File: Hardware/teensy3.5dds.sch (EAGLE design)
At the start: 101 parts, among them IC1 AD8034, IC10 AD8034, IC11 AD8034, IC12 AD8034, IC2 AD8034, IC4 AD737KRZ-R7, IC8 AD8034, IC9 AD8034, J1 1776275-2, J2 1776275-2, Q1 CSM-7X-DU, X1 1-227161-0

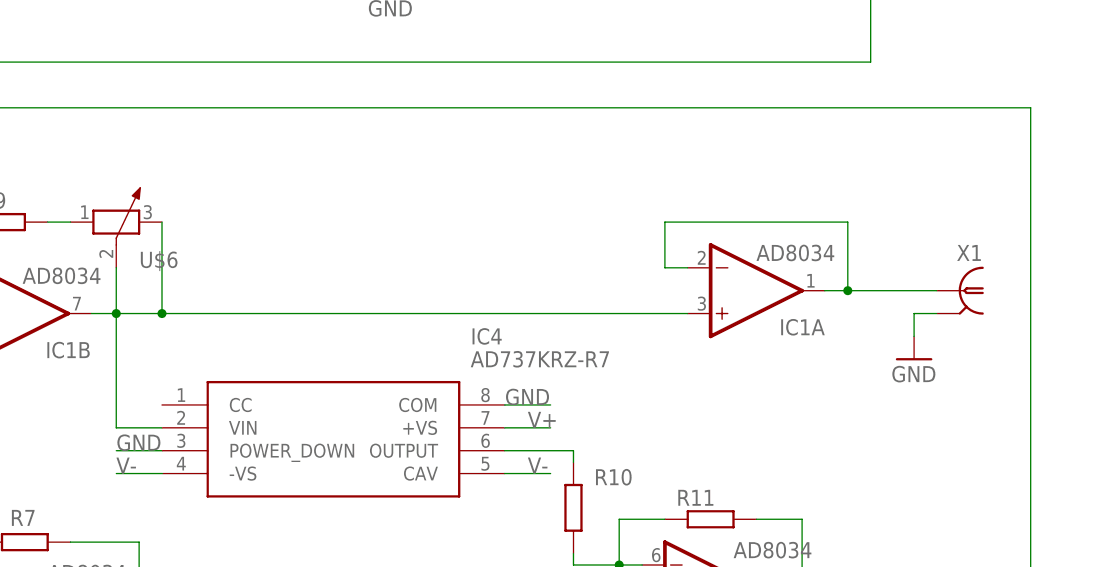
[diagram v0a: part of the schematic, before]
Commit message: hardware: add 50 Ohm resistor before BNC connector
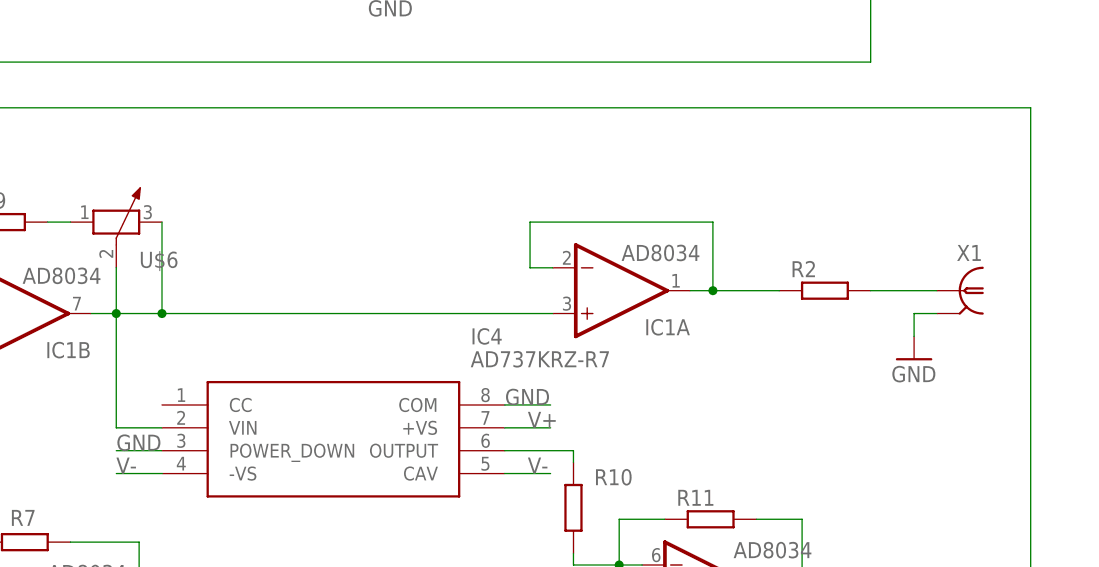
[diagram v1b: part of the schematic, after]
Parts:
- added R2: (no value), rcl:R-EU_R0805
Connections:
- new net N$6: R2.2, X1.1
- net N$19: now also R2.1; no longer X1.1
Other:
- moved on the sheet: IC1A
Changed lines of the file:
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@@
 <setting verticaltext="up"/>
 </settings>
-<grid distance="0.1" unitdist="inch" unit="inch" style="lines" multiple="1" display="yes" altdistance="0.05" altunitdist="inch" altunit="inch"/>
+<grid distance="0.1" unitdist="inch" unit="inch" style="lines" multiple="1" display="yes" altdistance="0.01" altunitdist="inch" altunit="inch"/>
 <layers>
 <layer number="1" name="Top" color="4" fill="1" visible="no" active="no"/>
@@
 <part name="GND10" library="supply1" library_urn="urn:adsk.eagle:library:371" deviceset="GND" device=""/>
 <part name="GND18" library="supply1" library_urn="urn:adsk.eagle:library:371" deviceset="GND" device=""/>
+<part name="R2" library="rcl" library_urn="urn:adsk.eagle:library:334" deviceset="R-EU_" device="R0805" package3d_urn="urn:adsk.eagle:package:23553/2"/>
 </parts>
 <sheets>
@@
 <attribute name="VALUE" x="35.56" y="-213.36" size="1.778" layer="96"/>
 </instance>
-<instance part="IC1" gate="A" x="322.58" y="-81.28" smashed="yes" rot="MR180">
-<attribute name="NAME" x="325.12" y="-84.455" size="1.778" layer="95" rot="MR180"/>
-<attribute name="VALUE" x="322.58" y="-76.2" size="1.778" layer="96" rot="MR180"/>
+<instance part="IC1" gate="A" x="307.594" y="-81.28" smashed="yes" rot="MR180">
+<attribute name="NAME" x="310.134" y="-84.455" size="1.778" layer="95" rot="MR180"/>
+<attribute name="VALUE" x="307.594" y="-76.2" size="1.778" layer="96" rot="MR180"/>
 </instance>
 <instance part="IC1" gate="B" x="241.046" y="-83.82" smashed="yes" rot="MR180">
@@
 <instance part="GND18" gate="1" x="-25.4" y="7.62" smashed="yes">
 <attribute name="VALUE" x="-27.94" y="5.08" size="1.778" layer="96"/>
+</instance>
+<instance part="R2" gate="G$1" x="330.2" y="-81.28" smashed="yes">
+<attribute name="NAME" x="326.39" y="-79.7814" size="1.778" layer="95"/>
+<attribute name="VALUE" x="326.39" y="-84.582" size="1.778" layer="96"/>
 </instance>
 </instances>
@@
 <wire x1="248.666" y1="-83.82" x2="251.46" y2="-83.82" width="0.1524" layer="91"/>
 <pinref part="IC1" gate="A" pin="+IN"/>
-<wire x1="256.54" y1="-83.82" x2="314.96" y2="-83.82" width="0.1524" layer="91"/>
+<wire x1="256.54" y1="-83.82" x2="299.974" y2="-83.82" width="0.1524" layer="91"/>
 <junction x="256.54" y="-83.82"/>
 </segment>
@@
 <segment>
 <pinref part="IC1" gate="A" pin="-IN"/>
-<wire x1="314.96" y1="-78.74" x2="312.42" y2="-78.74" width="0.1524" layer="91"/>
-<wire x1="312.42" y1="-78.74" x2="312.42" y2="-73.66" width="0.1524" layer="91"/>
+<wire x1="299.974" y1="-78.74" x2="297.434" y2="-78.74" width="0.1524" layer="91"/>
+<wire x1="297.434" y1="-78.74" x2="297.434" y2="-73.66" width="0.1524" layer="91"/>
+<pinref part="IC1" gate="A" pin="OUT"/>
+<wire x1="317.754" y1="-81.28" x2="315.214" y2="-81.28" width="0.1524" layer="91"/>
+<wire x1="297.434" y1="-73.66" x2="317.754" y2="-73.66" width="0.1524" layer="91"/>
+<wire x1="317.754" y1="-73.66" x2="317.754" y2="-81.28" width="0.1524" layer="91"/>
+<junction x="317.754" y="-81.28"/>
+<wire x1="325.12" y1="-81.28" x2="317.754" y2="-81.28" width="0.1524" layer="91"/>
+<pinref part="R2" gate="G$1" pin="1"/>
+</segment>
+</net>
+<net name="N$6" class="1">
+<segment>
 <pinref part="X1" gate="G$1" pin="1"/>
-<pinref part="IC1" gate="A" pin="OUT"/>
-<wire x1="342.646" y1="-81.28" x2="332.74" y2="-81.28" width="0.1524" layer="91"/>
-<wire x1="332.74" y1="-81.28" x2="330.2" y2="-81.28" width="0.1524" layer="91"/>
-<wire x1="312.42" y1="-73.66" x2="332.74" y2="-73.66" width="0.1524" layer="91"/>
-<wire x1="332.74" y1="-73.66" x2="332.74" y2="-81.28" width="0.1524" layer="91"/>
-<junction x="332.74" y="-81.28"/>
-</segment>
-</net>
+<wire x1="342.646" y1="-81.28" x2="335.28" y2="-81.28" width="0.1524" layer="91"/>
+<pinref part="R2" gate="G$1" pin="2"/>
+</segment>
+</net>

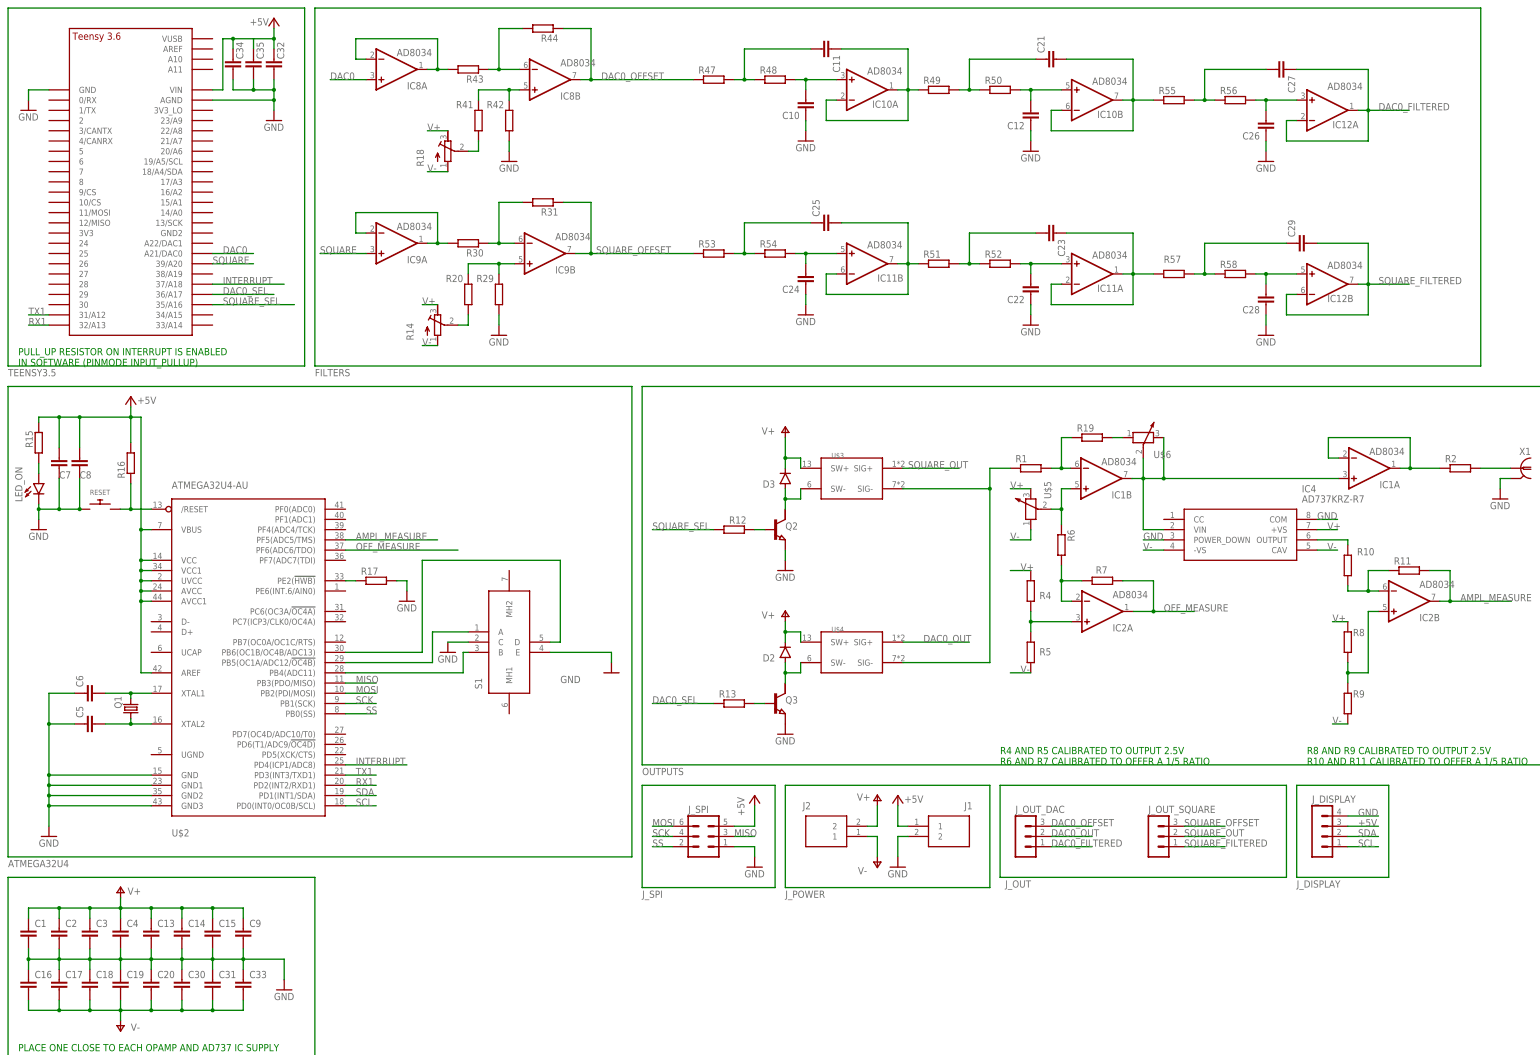
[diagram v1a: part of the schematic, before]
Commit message: hardware: renumber parts * Label power connector on board
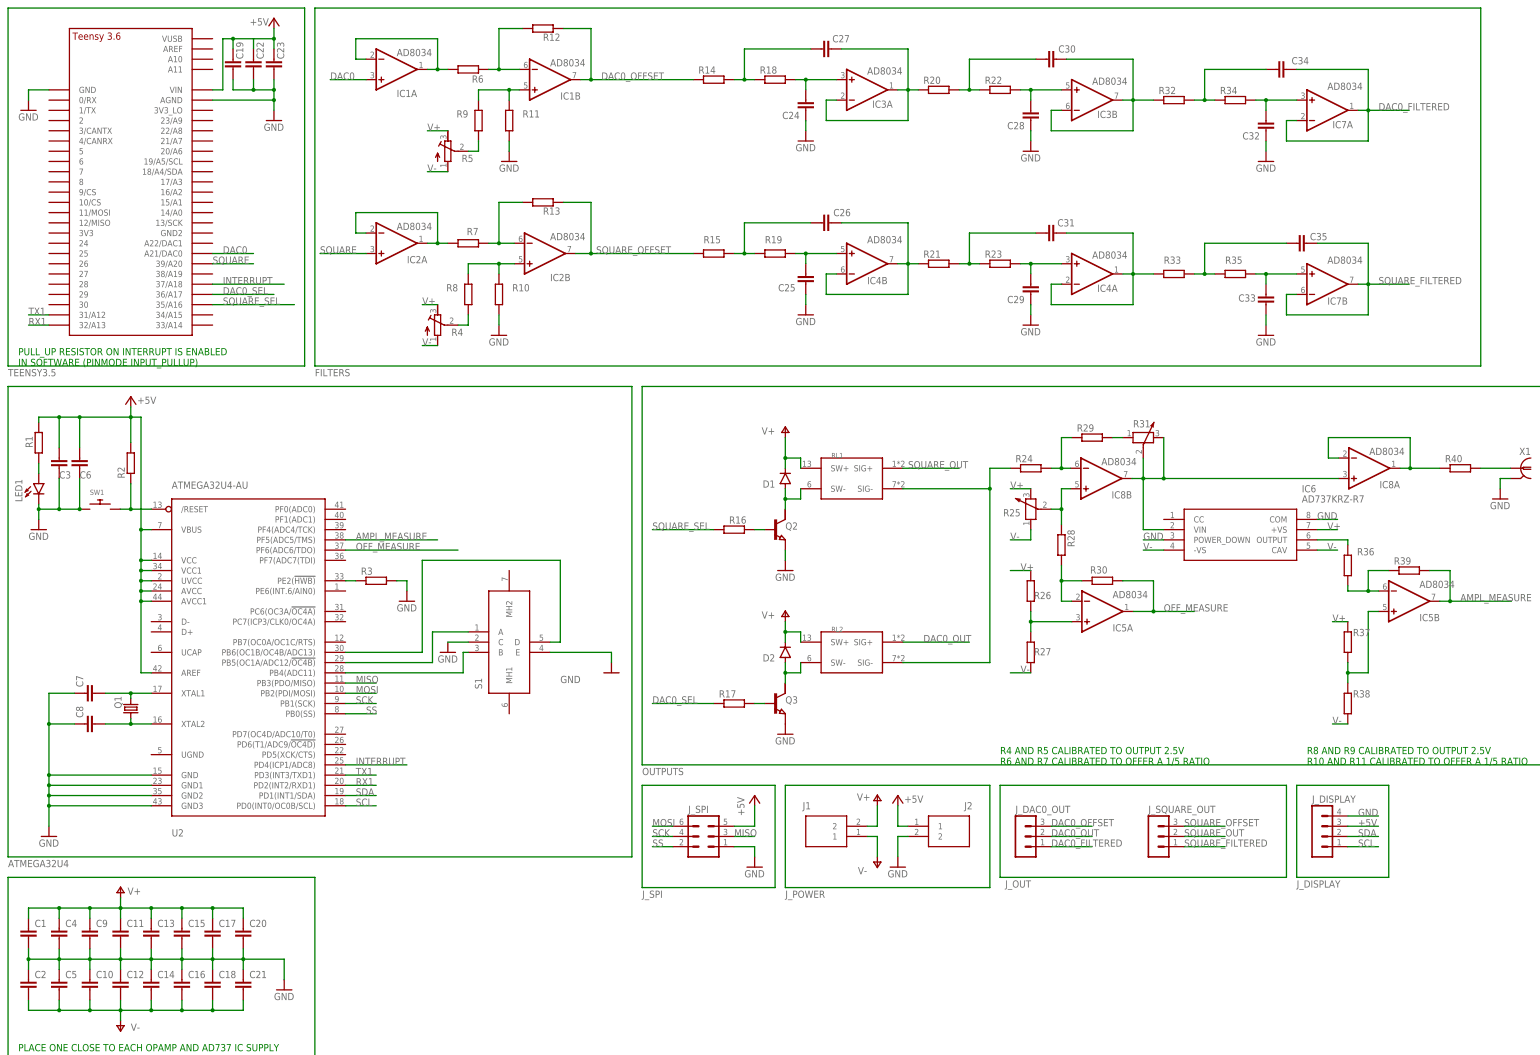
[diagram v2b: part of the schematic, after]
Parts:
- removed IC11, IC9: AD8034, linear:TL082D
- removed R41, R42, R43, R44, R47, R48: (no value), rcl:R-EU_R0805
- removed R49, R53, R54: (no value), rcl:R-EU_M0805
- removed U$6: POTENTIOMETER_VERTICAL, Potentiometer_vertical:POTENTIOMETER_VERTICAL
- added IC5: AD8034, linear:TL082D
- added IC6: AD737KRZ-R7, AD737KRZ-R7:AD737KRZ-R7
- added R24, R26, R27, R28, R36, R37, R38, R39, R40: (no value), rcl:R-EU_R0805
- added R3: 10kOhm, rcl:R-EU_M0805
- C19: value (none) -> 100n; device rcl:C-EUC0805 -> rcl:C-EUC1206
- C22, C23: value (none) -> 100n
- C3: value (none) -> 1u; device rcl:C-EUC0805 -> rcl:C-EUC1206
- C32, C35: value 100n -> (none)
- C34: value 100n -> (none); device rcl:C-EUC1206 -> rcl:C-EUC0805
- C5: value 22pF -> (none)
- C6: value 22pF -> 1u
- C7: value 1u -> 22pF; device rcl:C-EUC1206 -> rcl:C-EUC0805
- C8: value 1u -> 22pF
- IC4: value AD737KRZ-R7 -> AD8034; device AD737KRZ-R7:AD737KRZ-R7 -> linear:TL082D
- R1: value (none) -> 220Ohm; device rcl:R-EU_R0805 -> rcl:R-EU_M0805
- R12, R13: device rcl:R-EU_M0805 -> rcl:R-EU_R0805
- R14, R18: device rcl:R-TRIMM3296W -> rcl:R-EU_R0805
- R15: value 220Ohm -> (none)
- R16: value 10kOhm -> (none); device rcl:R-EU_R0805 -> rcl:R-EU_M0805
- R17: value 10kOhm -> (none)
- R19, R20: device rcl:R-EU_R0805 -> rcl:R-EU_M0805
- R2: value (none) -> 10kOhm
- R31: value (none) -> POTENTIOMETER_VERTICAL; device rcl:R-EU_R0805 -> Potentiometer_vertical:POTENTIOMETER_VERTICAL
- R4, R5: device rcl:R-EU_R0805 -> rcl:R-TRIMM3296W
- renumbered D3 to D1, IC10 to IC3, IC12 to IC7, J_OUT_DAC to J_DAC0_OUT, J_OUT_SQUARE to J_SQUARE_OUT, LED_ON to LED1, R50 to R22, R51 to R21, R52 to R23, R55 to R32, R56 to R34, R57 to R33, R58 to R35, RESET to SW1, U$1 to U1, U$2 to U2, U$3 to RL1, U$4 to RL2, U$5 to R25
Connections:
- net +5V: now also C19.1, C22.1, C23.1, C3.1, C6.1, J2.1, R1.2, R2.2; no longer C32.1, C34.1, C35.1, C7.1, C8.1, J1.1, R15.2, R16.2
- net AMPL_MEASURE: now also IC5B.OUT, R39.2; no longer IC2B.OUT, R11.2
- net DAC0: now also IC1A.+IN; no longer IC8A.+IN
- net DAC0_FILTERED: now also C34.1; no longer C27.1
- net DAC0_OFFSET: now also IC1B.OUT, R12.1, R14.1; no longer IC8B.OUT, R44.1, R47.1
- net DAC0_SEL: now also R17.1; no longer R13.1
- net GND: now also C11.2, C14.1, C17.2, C19.2, C2.1, C20.2, C21.1, C22.2, C23.2, C25.1, C29.1, C32.1, C6.2, C7.1, C8.1, IC6.COM, IC6.POWER_DOWN, J2.2, R10.1, R11.1, R3.2; no longer C14.2, C17.1, C19.1, C2.2, C20.1, C22.1, C26.1, C30.1, C31.1, C32.2, C34.2, C35.2, C6.1, C7.2, C8.2, IC4.COM, IC4.POWER_DOWN, J1.2, R17.2, R29.1, R42.1
- net N$10: now also R24.1; no longer R1.1
- net N$11: now also IC5A.-IN, R28.2, R30.2; no longer IC2A.-IN, R6.2, R7.2
- net N$13: now also IC5A.+IN, R26.1, R27.2; no longer IC2A.+IN, R4.1, R5.2
- net N$14: now also IC6.OUTPUT, R36.1; no longer IC4.OUTPUT, R10.1
- net N$15: now also R29.2, R31.1; no longer R19.2, U$6.1
- net N$16: now also IC5B.-IN, R36.2, R39.1; no longer IC2B.-IN, R10.2, R11.1
- net N$17: now also R16.2; no longer R12.2
- net N$18: now also R17.2; no longer R13.2
- net N$19: now also IC8A.-IN, IC8A.OUT, R40.1; no longer IC1A.-IN, IC1A.OUT, R2.1
- net N$22: now also IC5B.+IN, R37.2, R38.1; no longer IC2B.+IN, R8.2, R9.1
- net N$3: now also IC8B.+IN, R28.1; no longer IC1B.+IN, R6.1
- net N$30: now also R1.1; no longer R15.1
- net N$31: now also C7.2; no longer C6.2
- net N$32: now also R3.1; no longer R17.1
- net N$35: now also R2.1; no longer R16.1
- net N$38: now also IC2A.-IN, IC2A.OUT, R7.2; no longer IC9A.-IN, IC9A.OUT, R30.2
- net N$4: now also C8.2; no longer C5.2
- net N$41: now also IC1A.-IN, IC1A.OUT, R6.2; no longer IC8A.-IN, IC8A.OUT, R43.2
- net N$5: now also IC8B.-IN, R24.2, R29.1; no longer IC1B.-IN, R1.2, R19.1
- net N$50: now also C27.2, R14.2, R18.1; no longer C11.2, R47.2, R48.1
- net N$51: now also IC1B.-IN, R12.2, R6.1; no longer IC8B.-IN, R43.1, R44.2
- net N$53: now also C27.1, R20.1; no longer C11.1, R49.1
- net N$54: now also IC1B.+IN, R11.2, R9.2; no longer IC8B.+IN, R41.2, R42.2
- net N$56: now also R5.S, R9.1; no longer R18.S, R41.1
- net N$57: now also IC2B.-IN, R13.2, R7.1; no longer IC9B.-IN, R30.1, R31.2
- net N$58: now also C24.2, R18.2; no longer C10.2, R48.2
- net N$59: now also IC2B.+IN, R10.2, R8.2; no longer IC9B.+IN, R20.2, R29.2
- net N$6: now also R40.2; no longer R2.2
- net N$60: now also R4.S, R8.1; no longer R14.S, R20.1
- net N$61: now also C30.1, R20.2; no longer C21.1, R49.2
- net N$62: now also C30.2; no longer C21.2
- net N$63: now also C28.2; no longer C12.2
- net N$66: now also C31.2; no longer C23.2
- net N$67: now also C31.1, IC4A.-IN, IC4A.OUT; no longer C23.1, IC11A.-IN, IC11A.OUT
- net N$68: now also C29.2, IC4A.+IN; no longer C22.2, IC11A.+IN
- net N$69: now also C26.1, R15.2, R19.1; no longer C25.1, R53.2, R54.1
- net N$70: now also C26.2, IC4B.-IN, IC4B.OUT; no longer C25.2, IC11B.-IN, IC11B.OUT
- net N$71: now also C25.2, IC4B.+IN, R19.2; no longer C24.2, IC11B.+IN, R54.2
- net N$73: now also C34.2; no longer C27.2
- net N$75: now also C32.2; no longer C26.2
- net N$76: now also C35.1; no longer C29.1
- net N$78: now also C33.2; no longer C28.2
- net N$9: now also IC6.VIN, IC8A.+IN, IC8B.OUT, R31.2, R31.3; no longer IC1A.+IN, IC1B.OUT, IC4.VIN, U$6.2, U$6.3
- net OFF_MEASURE: now also IC5A.OUT, R30.1; no longer IC2A.OUT, R7.1
- net SQUARE: now also IC2A.+IN; no longer IC9A.+IN
- net SQUARE_FILTERED: now also C35.2; no longer C29.2
- net SQUARE_OFFSET: now also IC2B.OUT, R13.1, R15.1; no longer IC9B.OUT, R31.1, R53.1
- net SQUARE_SEL: now also R16.1; no longer R12.1
- net V+: now also C11.1, C17.1, C20.1, IC6.+VS, J1.2, R26.2, R37.1, R4.E, R5.E; no longer C14.1, C2.1, C3.1, IC4.+VS, J2.2, R14.E, R18.E, R4.2, R8.1
- net V-: now also C10.2, C12.2, C14.2, C2.2, C21.2, C5.2, IC6.-VS, IC6.CAV, J1.1, R27.1, R38.2, R4.A, R5.A; no longer C17.2, C19.2, C20.2, C30.2, C31.2, C33.2, IC4.-VS, IC4.CAV, J2.1, R14.A, R18.A, R5.1, R9.2
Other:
- moved on the sheet: C10, C11, C12, C14, C15, C16, C17, C18, C19, C2, C20, C21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

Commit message: little fixes
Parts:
- added R41, R42, R43: (no value), rcl:R-EU_R0805
- C1, C10, C12, C13, C14, C15, C16, C17, C18, C2, C20, C21, C4, C5, C9: value (none) -> 100n
- C23: value 100n -> 1u
- C24, C25, C28, C29, C32, C33: value (none) -> 10p
- C26, C27, C30, C31, C34, C35: value (none) -> 100p
- C6: value 1u -> 100n
- C7, C8: value 22pF -> 22p
- Q1: value CSM-7X-DU -> 10MHz
- R1: value 220Ohm -> 220
- R10, R11, R12, R24, R6, R7, R8, R9: value (none) -> 1k
- R13: value (none) -> 100k; device rcl:R-EU_R0805 -> rcl:R-TRIMM3296W
- R14, R18: value (none) -> 2.74k
- R15: value (none) -> 130
- R19: value (none) -> 4.75k
- R2, R3: value 10kOhm -> 10k
- R20: value (none) -> 787
- R21: value (none) -> 150
- R22: value (none) -> 14.3k
- R23: value (none) -> 3.74k
- R25, R31: value POTENTIOMETER_VERTICAL -> 10k
- R29: value (none) -> 100
- R32: value (none) -> 562
- R33: value (none) -> 243
- R34: value (none) -> 20k
- R35: value (none) -> 1.78k
- R4: value (none) -> 1k; device rcl:R-TRIMM3296W -> rcl:R-EU_R0805
- R40: value (none) -> 50
- R5: value (none) -> 100k
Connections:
- removed net N$1: S1.B, U2.PB4(ADC11)
- removed net N$38: IC2A.-IN, IC2A.OUT, R7.2
- removed net N$41: IC1A.-IN, IC1A.OUT, R6.2
- removed net N$57: IC2B.-IN, R13.2, R7.1
- removed net N$59: IC2B.+IN, R10.2, R8.2
- removed net N$60: R4.S, R8.1
- new net N$20: R13.S, R4.1
- new net N$23: IC1A.-IN, IC1A.OUT, R11.1
- new net N$24: IC2B.-IN, R10.2, R8.1
- new net N$27: IC2A.-IN, IC2A.OUT, R7.1
- new net N$28: IC2B.+IN, R4.2, R7.2
- new net N$29: R43.2, S1.SW, U2.PB5(OC1A/ADC12/!OC4B)
- new net V-1: R13.A
- net +5V: now also R41.1, R42.1
- net GND: now also R43.1, R6.2, R8.2, S1.MH1, S1.MH2; no longer R10.1, R11.1
- net N$25: now also R41.2, S1.A; no longer S1.D
- net N$8: now also R42.2, S1.B, U2.PB7(OC0A/OC1C/RTS); no longer S1.A, U2.PB5(OC1A/ADC12/!OC4B)
- net SQUARE_OFFSET: now also R10.1; no longer R13.1
- net V+: now also R13.E; no longer R4.E
- net V-: no longer R4.A
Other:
- moved on the sheet: C24, C27, C28, C30, C32, C34, C35, D1, D2, IC1A, IC1B, IC2A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
